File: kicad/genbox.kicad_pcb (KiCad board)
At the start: 2 copper layers, 336 x 134 mm, 56 parts, among them J1 USB_A, SW15 SW_SPST, SW16 SW_SPST, SW17 SW_SPST, SW18 SW_SPST, U1 DM-OLED096-636, U2 rp2040-zero, U3 SN74LV1T34DBV

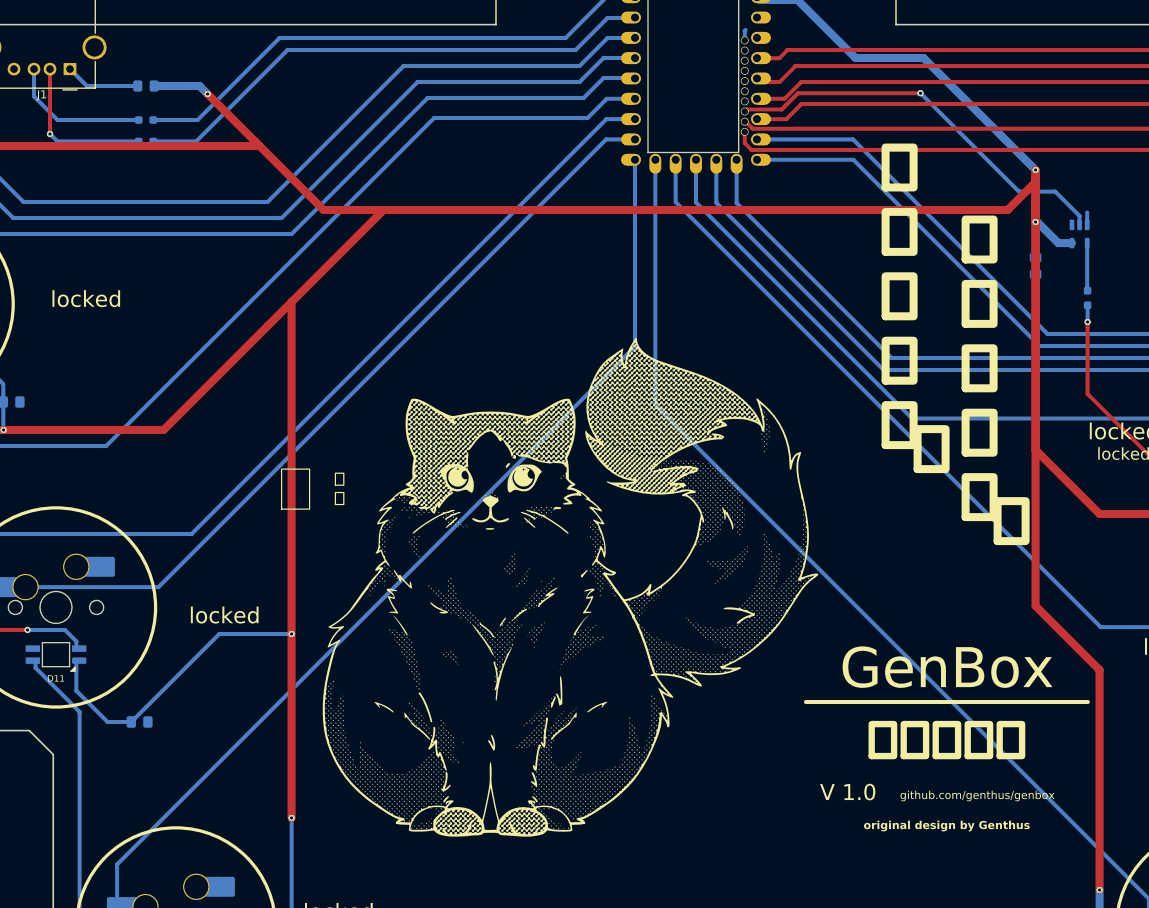
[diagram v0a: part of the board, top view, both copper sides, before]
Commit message: pcb handsolder adjustments
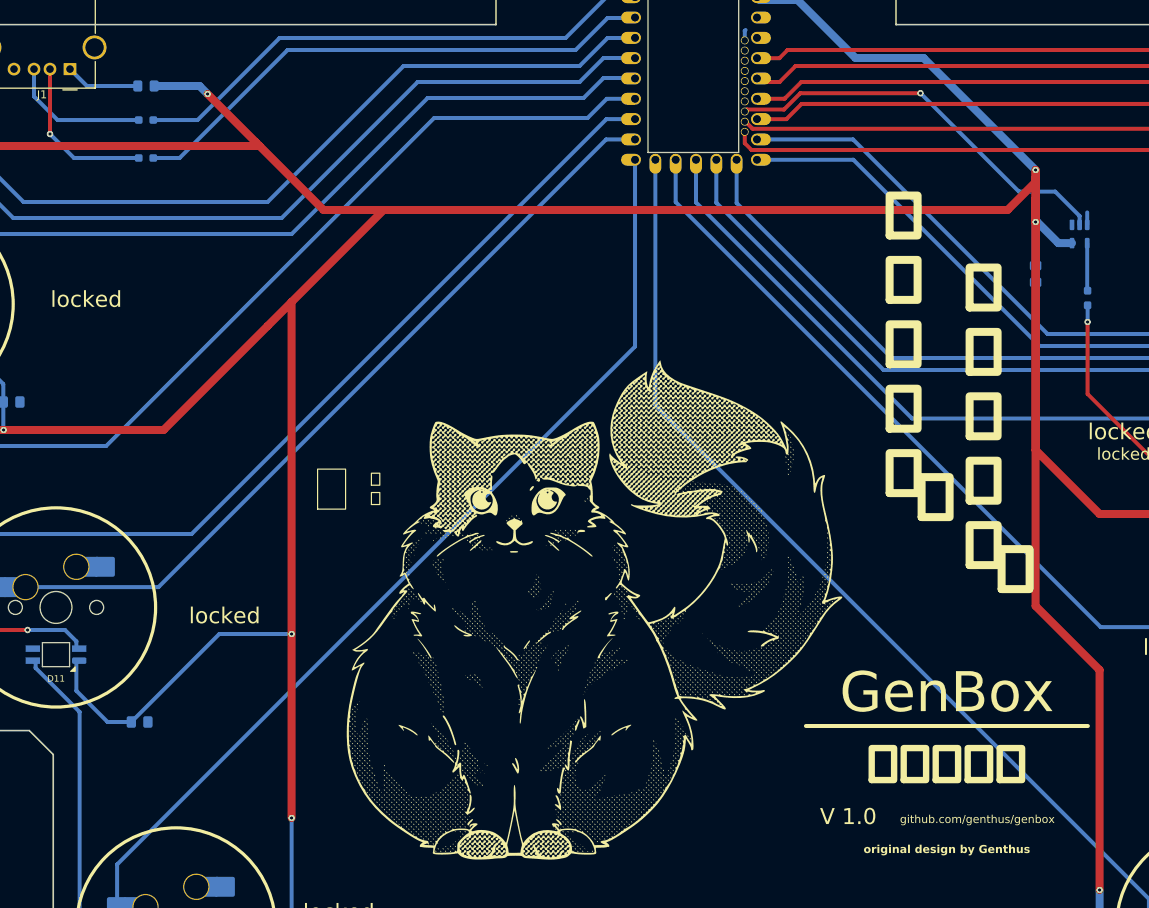
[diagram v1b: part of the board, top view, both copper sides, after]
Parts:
- moved G*** 4.15 mm to (200.0, 120.9)
- moved R1 2.07 mm to (143.8, 63.5)
- moved C1 1.00 mm to (255.0, 78.0)
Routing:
- net +5V: track 1107.1 -> 1108.1 mm
- net USBA D-: track 66.6 -> 67.5 mm
- net Net-(J1-D-): track 19.6 -> 20.4 mm

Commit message: reworked 5+v traces
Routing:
- net +5V: track 1108.1 -> 241.7 mm, vias 12 -> 18
- added copper zone on F.Cu, net +5V

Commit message: added mounting holes
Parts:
- added REF1: MountingHole_4mm, MountingHole:MountingHole_4mm, F.Cu at (152.6, 54.3)
- added REF2: MountingHole_4mm, MountingHole:MountingHole_4mm, F.Cu at (272.6, 54.3)
- added REF3: MountingHole_3.5mm, MountingHole:MountingHole_3.5mm, F.Cu at (152.6, 124.7)
- added REF4: MountingHole_3.5mm, MountingHole:MountingHole_3.5mm, F.Cu at (272.6, 124.7)
- moved R2 1.24 mm to (143.8, 60.0)
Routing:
- net S2: track 113.0 -> 117.2 mm
- net A1: track 134.0 -> 136.1 mm
- net S1: track 91.8 -> 93.4 mm
- net A2: track 154.2 -> 155.5 mm
- net USBA D+: track 66.6 -> 67.1 mm
- net Net-(J1-D+): track 17.7 -> 18.2 mm
